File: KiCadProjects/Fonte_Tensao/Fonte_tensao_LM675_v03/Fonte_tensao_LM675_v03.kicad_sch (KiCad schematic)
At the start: 32 parts, among them J1 Barrel_Jack, J2 sinais analogicos, J3 comunicacao / sinais digitais, J4 tensoes, U1 L7809, U2 LM7909_TO220, U3 LM675, U4 L7805, U5 L7905, U6 LM1117T-3.3

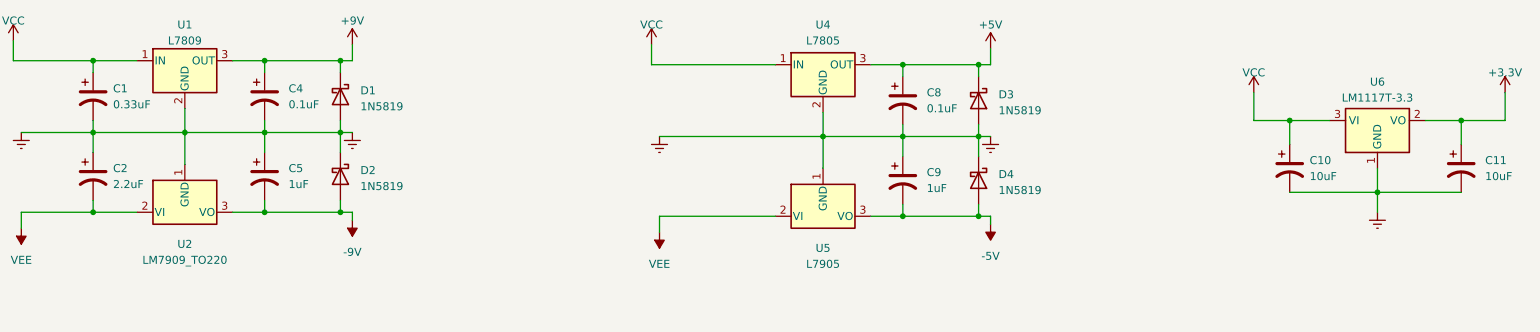
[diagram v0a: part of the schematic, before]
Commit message: atualizacao dos valores de capacitores (eletroliticos) da fonte de tensao
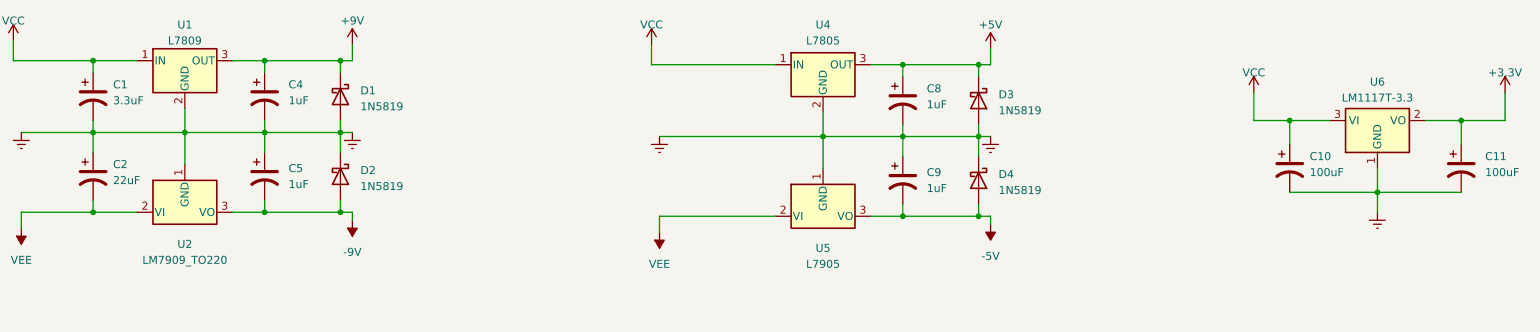
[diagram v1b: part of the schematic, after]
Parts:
- C1: value 0.33uF -> 3.3uF
- C10, C11: value 10uF -> 100uF
- C2: value 2.2uF -> 22uF
- C4, C8: value 0.1uF -> 1uF
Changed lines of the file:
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@@
     (company "EITduino")
     (comment 1 "Autor: Gustavo Pinheiro")
-    (comment 2 "reguladores: usar capacitores de tantalo")
     (comment 3 "Chave gangorra kcd1 no lugar do botao para acionamento")
   )
@@
   (symbol (lib_id "Device:C_Polarized_US") (at 72.39 38.1 0) (unit 1)
     (in_bom yes) (on_board yes) (dnp no) (fields_autoplaced)
-    (property "Reference" "C4" (at 76.2 36.83 0)
-      (effects (font (size 1.27 1.27)) (justify left))
-    )
-    (property "Value" "0.1uF" (at 76.2 39.37 0)
+    (property "Reference" "C4" (at 76.2 36.195 0)
+      (effects (font (size 1.27 1.27)) (justify left))
+    )
+    (property "Value" "1uF" (at 76.2 38.735 0)
       (effects (font (size 1.27 1.27)) (justify left))
     )
@@
   (symbol (lib_id "Device:C_Polarized_US") (at 235.585 49.53 0) (unit 1)
     (in_bom yes) (on_board yes) (dnp no) (fields_autoplaced)
-    (property "Reference" "C10" (at 238.76 48.26 0)
-      (effects (font (size 1.27 1.27)) (justify left))
-    )
-    (property "Value" "10uF" (at 238.76 50.8 0)
+    (property "Reference" "C10" (at 238.76 47.625 0)
+      (effects (font (size 1.27 1.27)) (justify left))
+    )
+    (property "Value" "100uF" (at 238.76 50.165 0)
       (effects (font (size 1.27 1.27)) (justify left))
     )
@@
   (symbol (lib_id "Device:C_Polarized_US") (at 45.085 50.8 0) (unit 1)
     (in_bom yes) (on_board yes) (dnp no) (fields_autoplaced)
-    (property "Reference" "C2" (at 48.26 49.53 0)
-      (effects (font (size 1.27 1.27)) (justify left))
-    )
-    (property "Value" "2.2uF" (at 48.26 52.07 0)
+    (property "Reference" "C2" (at 48.26 48.895 0)
+      (effects (font (size 1.27 1.27)) (justify left))
+    )
+    (property "Value" "22uF" (at 48.26 51.435 0)
       (effects (font (size 1.27 1.27)) (justify left))
     )
@@
   (symbol (lib_id "Device:C_Polarized_US") (at 45.085 38.1 0) (unit 1)
     (in_bom yes) (on_board yes) (dnp no) (fields_autoplaced)
-    (property "Reference" "C1" (at 48.26 36.83 0)
-      (effects (font (size 1.27 1.27)) (justify left))
-    )
-    (property "Value" "0.33uF" (at 48.26 39.37 0)
+    (property "Reference" "C1" (at 48.26 36.195 0)
+      (effects (font (size 1.27 1.27)) (justify left))
+    )
+    (property "Value" "3.3uF" (at 48.26 38.735 0)
       (effects (font (size 1.27 1.27)) (justify left))
     )
@@
   (symbol (lib_id "Device:C_Polarized_US") (at 262.89 49.53 0) (unit 1)
     (in_bom yes) (on_board yes) (dnp no) (fields_autoplaced)
-    (property "Reference" "C11" (at 266.7 48.26 0)
-      (effects (font (size 1.27 1.27)) (justify left))
-    )
-    (property "Value" "10uF" (at 266.7 50.8 0)
+    (property "Reference" "C11" (at 266.7 47.625 0)
+      (effects (font (size 1.27 1.27)) (justify left))
+    )
+    (property "Value" "100uF" (at 266.7 50.165 0)
       (effects (font (size 1.27 1.27)) (justify left))
     )
@@
   (symbol (lib_id "Device:C_Polarized_US") (at 173.99 38.735 0) (unit 1)
     (in_bom yes) (on_board yes) (dnp no) (fields_autoplaced)
-    (property "Reference" "C8" (at 177.8 37.465 0)
-      (effects (font (size 1.27 1.27)) (justify left))
-    )
-    (property "Value" "0.1uF" (at 177.8 40.005 0)
-      (effects (font (size 1.27 1.27)) (justify left))
-    )
+    (property "Reference" "C8" (at 177.8 36.83 0)
+      (effects (font (size 1.27 1.27)) (justify left))
+    )
+    (property "Value" "1uF" (at 177.8 39.37 0)
+      (effects (font (size 1.27 1.27)) (justify left))
+    )

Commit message: revisar alteracoes fonte tensao v3
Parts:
- C1: value 3.3uF -> 0.33uF
- C10, C11: value 100uF -> 10uF
- C2: value 22uF -> 2.2uF
- C4, C8: value 1uF -> 0.1uF
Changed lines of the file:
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@@
     (company "EITduino")
     (comment 1 "Autor: Gustavo Pinheiro")
+    (comment 2 "reguladores: usar capacitores de tantalo")
     (comment 3 "Chave gangorra kcd1 no lugar do botao para acionamento")
   )
@@
   (symbol (lib_id "Device:C_Polarized_US") (at 72.39 38.1 0) (unit 1)
     (in_bom yes) (on_board yes) (dnp no) (fields_autoplaced)
-    (property "Reference" "C4" (at 76.2 36.195 0)
-      (effects (font (size 1.27 1.27)) (justify left))
-    )
-    (property "Value" "1uF" (at 76.2 38.735 0)
+    (property "Reference" "C4" (at 76.2 36.83 0)
+      (effects (font (size 1.27 1.27)) (justify left))
+    )
+    (property "Value" "0.1uF" (at 76.2 39.37 0)
       (effects (font (size 1.27 1.27)) (justify left))
     )
@@
   (symbol (lib_id "Device:C_Polarized_US") (at 235.585 49.53 0) (unit 1)
     (in_bom yes) (on_board yes) (dnp no) (fields_autoplaced)
-    (property "Reference" "C10" (at 238.76 47.625 0)
-      (effects (font (size 1.27 1.27)) (justify left))
-    )
-    (property "Value" "100uF" (at 238.76 50.165 0)
+    (property "Reference" "C10" (at 238.76 48.26 0)
+      (effects (font (size 1.27 1.27)) (justify left))
+    )
+    (property "Value" "10uF" (at 238.76 50.8 0)
       (effects (font (size 1.27 1.27)) (justify left))
     )
@@
   (symbol (lib_id "Device:C_Polarized_US") (at 45.085 50.8 0) (unit 1)
     (in_bom yes) (on_board yes) (dnp no) (fields_autoplaced)
-    (property "Reference" "C2" (at 48.26 48.895 0)
-      (effects (font (size 1.27 1.27)) (justify left))
-    )
-    (property "Value" "22uF" (at 48.26 51.435 0)
+    (property "Reference" "C2" (at 48.26 49.53 0)
+      (effects (font (size 1.27 1.27)) (justify left))
+    )
+    (property "Value" "2.2uF" (at 48.26 52.07 0)
       (effects (font (size 1.27 1.27)) (justify left))
     )
@@
   (symbol (lib_id "Device:C_Polarized_US") (at 45.085 38.1 0) (unit 1)
     (in_bom yes) (on_board yes) (dnp no) (fields_autoplaced)
-    (property "Reference" "C1" (at 48.26 36.195 0)
-      (effects (font (size 1.27 1.27)) (justify left))
-    )
-    (property "Value" "3.3uF" (at 48.26 38.735 0)
+    (property "Reference" "C1" (at 48.26 36.83 0)
+      (effects (font (size 1.27 1.27)) (justify left))
+    )
+    (property "Value" "0.33uF" (at 48.26 39.37 0)
       (effects (font (size 1.27 1.27)) (justify left))
     )
@@
   (symbol (lib_id "Device:C_Polarized_US") (at 262.89 49.53 0) (unit 1)
     (in_bom yes) (on_board yes) (dnp no) (fields_autoplaced)
-    (property "Reference" "C11" (at 266.7 47.625 0)
-      (effects (font (size 1.27 1.27)) (justify left))
-    )
-    (property "Value" "100uF" (at 266.7 50.165 0)
+    (property "Reference" "C11" (at 266.7 48.26 0)
+      (effects (font (size 1.27 1.27)) (justify left))
+    )
+    (property "Value" "10uF" (at 266.7 50.8 0)
       (effects (font (size 1.27 1.27)) (justify left))
     )
@@
   (symbol (lib_id "Device:C_Polarized_US") (at 173.99 38.735 0) (unit 1)
     (in_bom yes) (on_board yes) (dnp no) (fields_autoplaced)
-    (property "Reference" "C8" (at 177.8 36.83 0)
-      (effects (font (size 1.27 1.27)) (justify left))
-    )
-    (property "Value" "1uF" (at 177.8 39.37 0)
-      (effects (font (size 1.27 1.27)) (justify left))
-    )
+    (property "Reference" "C8" (at 177.8 37.465 0)
+      (effects (font (size 1.27 1.27)) (justify left))
+    )
+    (property "Value" "0.1uF" (at 177.8 40.005 0)
+      (effects (font (size 1.27 1.27)) (justify left))
+    )
